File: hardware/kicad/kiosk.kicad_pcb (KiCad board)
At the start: 2 copper layers, 158 x 116 mm, 19 parts, among them J10 TerminalBlock_MaiXu_MX126-5.0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, J11 TerminalBlock_MaiXu_MX126-5.0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, J13 PinHeader_1x09_P2.54mm_Vertic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, J3 PinSocket_1x14_P2.54mm_Vertic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, J4 PinSocket_1x06_P2.54mm_Vertic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, J5 PinSocket_1x04_P2.54mm_Vertic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, J6 PinSocket_1x06_P2.54mm_Vertic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, J7 PinSocket_1x07_P2.54mm_Vertic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, J9 PinHeader_1x03_P2.54mm_Vertic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, U1 ESP32-S3-CAM

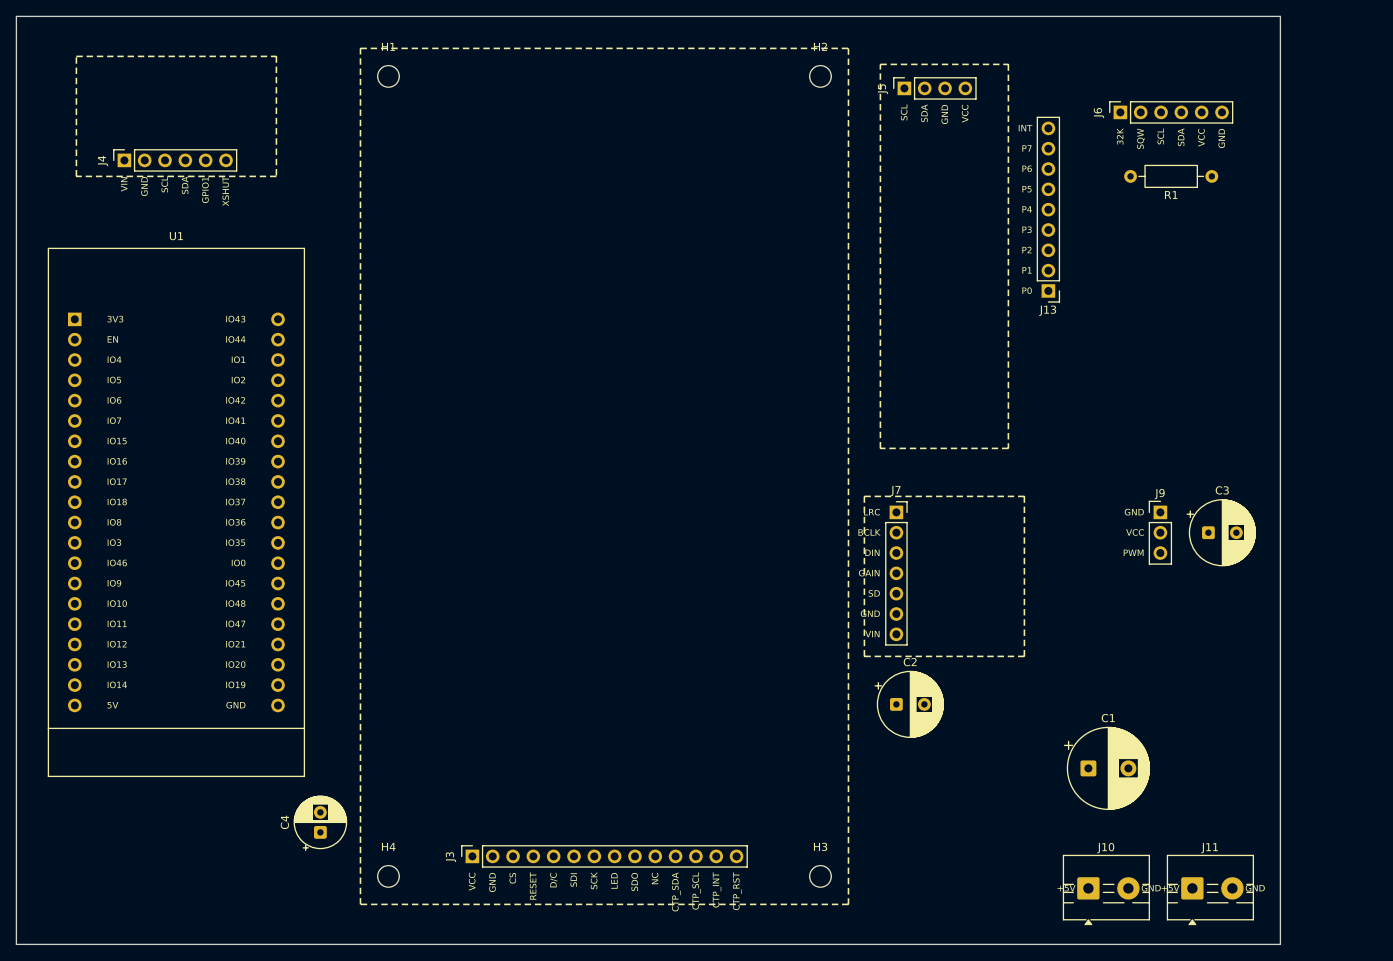
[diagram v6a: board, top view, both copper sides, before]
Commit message: fix(hardware): put the panel's header on the line its mounting holes sit on
Read off the module, the fourteen-pin row lands level with the two holes
at that end, about a millimetre nearer the edge. The board had it 2.5 mm
the other way. The two insets are therefore not independent: the header
one is now derived from the hole one, so the single measurement that is
still outstanding settles both at once, and there is no second number to
get wrong.

J3 drops to y 107.5 so the panel's far edge still clears the top of the
board. Its pin names now fall just below the panel's edge instead of
under it, which is where you want them: readable with the panel fitted.

Moving J11 inward last commit left the two supply terminals 1.5 mm apart,
and a label set beside a pad then reaches the neighbour: J10's GND landed
on J11's body, the same failure the outboard rule was written to fix. On
a two-pad row the label goes above its own pad now, nudged off the
reference text that sits centred between them.

Task: E14-T8
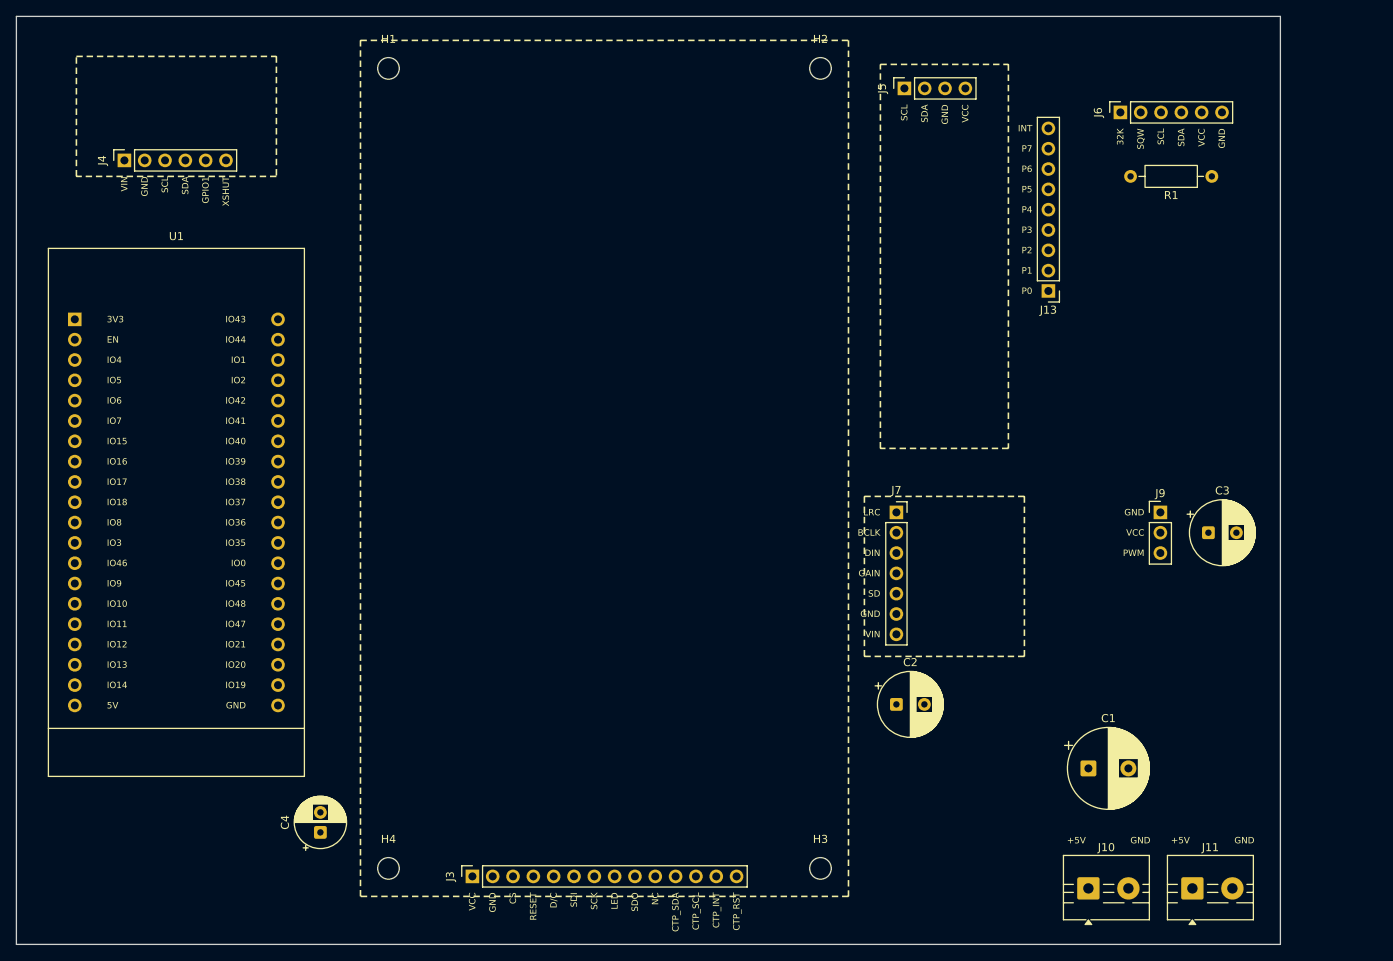
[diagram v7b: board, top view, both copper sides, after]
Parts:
- moved J3 2.50 mm to (57.0, 107.5)
- moved H1 1.00 mm to (46.5, 6.50)
- moved H2 1.00 mm to (100.5, 6.50)
- moved H3 1.00 mm to (100.5, 106.5)
- moved H4 1.00 mm to (46.5, 106.5)
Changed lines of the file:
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@@
 	(footprint "Connector_PinSocket_2.54mm:PinSocket_1x14_P2.54mm_Vertical"
 		(layer "F.Cu")
-		(at 57 105 90)
+		(at 57 107.5 90)
 		(descr "Through hole straight socket strip, 1x14, 2.54mm pitch, single row (from Kicad 4.0.7), script generated")
 		(tags "Through hole socket strip THT 1x14 2.54mm single row")
@@
 	(footprint "MountingHole:MountingHole_2.7mm"
 		(layer "F.Cu")
-		(at 100.51 7.5)
+		(at 100.51 6.5)
 		(descr "Mounting Hole 2.7mm, no annular, generated by kicad-footprint-generator mountinghole.py")
 		(tags "mountinghole")
@@
 	(footprint "MountingHole:MountingHole_2.7mm"
 		(layer "F.Cu")
-		(at 46.51 107.5)
+		(at 46.51 106.5)
 		(descr "Mounting Hole 2.7mm, no annular, generated by kicad-footprint-generator mountinghole.py")
 		(tags "mountinghole")
@@
 	(footprint "MountingHole:MountingHole_2.7mm"
 		(layer "F.Cu")
-		(at 100.51 107.5)
+		(at 100.51 106.5)
 		(descr "Mounting Hole 2.7mm, no annular, generated by kicad-footprint-generator mountinghole.py")
 		(tags "mountinghole")
@@
 	(footprint "MountingHole:MountingHole_2.7mm"
 		(layer "F.Cu")
-		(at 46.51 7.5)
+		(at 46.51 6.5)
 		(descr "Mounting Hole 2.7mm, no annular, generated by kicad-footprint-generator mountinghole.py")
 		(tags "mountinghole")
@@
 	)
 	(gr_line
-		(start 43.01 4)
-		(end 104.01 4)
+		(start 43.01 3)
+		(end 104.01 3)
 		(stroke
 			(width 0.2)
@@
 	)
 	(gr_line
-		(start 43.01 111)
-		(end 43.01 4)
+		(start 43.01 110)
+		(end 43.01 3)
 		(stroke
 			(width 0.2)
@@
 	)
 	(gr_line
-		(start 104.01 4)
-		(end 104.01 111)
+		(start 104.01 3)
+		(end 104.01 110)
 		(stroke
 			(width 0.2)
@@
 	)
 	(gr_line
-		(start 104.01 111)
-		(end 43.01 111)
+		(start 104.01 110)
+		(end 43.01 110)
 		(stroke
 			(width 0.2)
@@
 		)
 	)
+	(gr_text "+5V"
+		(at 132.5 103 0)
+		(layer "F.SilkS")
+		(effects
+			(font
+				(size 0.8 0.8)
+				(thickness 0.12)
+			)
+		)
+	)
 	(gr_text "GND"
-		(at 140.6 109 0)
+		(at 140.5 103 0)
+		(layer "F.SilkS")
+		(effects
+			(font
+				(size 0.8 0.8)
+				(thickness 0.12)
+			)
+		)
+	)
+	(gr_text "+5V"
+		(at 145.5 103 0)
 		(layer "F.SilkS")
 		(effects
@@
 				(thickness 0.12)
 			)
-			(justify left)
 		)
 	)
 	(gr_text "GND"
-		(at 153.6 109 0)
+		(at 153.5 103 0)
 		(layer "F.SilkS")
 		(effects
@@
 				(thickness 0.12)
 			)
-			(justify left)
 		)
 	)
@@
 		)
 	)
-	(gr_text "+5V"
-		(at 132.4 109 0)
-		(layer "F.SilkS")
-		(effects
-			(font
-				(size 0.8 0.8)
-				(thickness 0.12)
-			)
-			(justify right)
-		)
-	)
 	(gr_text "GND"
 		(at 141 62 0)
@@
 		)
 	)
-	(gr_text "+5V"
-		(at 145.4 109 0)
-		(layer "F.SilkS")
-		(effects
-			(font
-				(size 0.8 0.8)
-				(thickness 0.12)
-			)
-			(justify right)
-		)
-	)
 	(gr_text "VIN"
 		(at 13.5 20 90)
@@
 	)
 	(gr_text "VCC"
-		(at 57 107 90)
+		(at 57 109.5 90)
 		(layer "F.SilkS")
 		(effects
@@
 	)
 	(gr_text "GND"
-		(at 59.54 107 90)
+		(at 59.54 109.5 90)
 		(layer "F.SilkS")
 		(effects
@@
 	)
 	(gr_text "CS"
-		(at 62.08 107 90)
+		(at 62.08 109.5 90)
 		(layer "F.SilkS")
 		(effects
@@
 	)
 	(gr_text "RESET"
-		(at 64.62 107 90)
+		(at 64.62 109.5 90)
 		(layer "F.SilkS")
 		(effects
@@
 	)
 	(gr_text "D/C"
-		(at 67.16 107 90)
+		(at 67.16 109.5 90)
 		(layer "F.SilkS")
 		(effects
@@
 	)
 	(gr_text "SDI"
-		(at 69.7 107 90)
+		(at 69.7 109.5 90)
 		(layer "F.SilkS")
 		(effects
@@
 	)
 	(gr_text "SCK"
-		(at 72.24 107 90)
+		(at 72.24 109.5 90)
 		(layer "F.SilkS")
 		(effects
@@
 	)
 	(gr_text "LED"
-		(at 74.78 107 90)
+		(at 74.78 109.5 90)
 		(layer "F.SilkS")
 		(effects
@@
 	)
 	(gr_text "SDO"
-		(at 77.32 107 90)
+		(at 77.32 109.5 90)
 		(layer "F.SilkS")
 		(effects
@@
 	)
 	(gr_text "NC"
-		(at 79.86 107 90)
+		(at 79.86 109.5 90)
 		(layer "F.SilkS")
 		(effects
@@
 	)
 	(gr_text "CTP_SDA"
-		(at 82.4 107 90)
+		(at 82.4 109.5 90)
 		(layer "F.SilkS")
 		(effects
@@
 	)
 	(gr_text "CTP_SCL"
-		(at 84.94 107 90)
+		(at 84.94 109.5 90)
 		(layer "F.SilkS")
 		(effects
@@
 	)
 	(gr_text "CTP_INT"
-		(at 87.48 107 90)
+		(at 87.48 109.5 90)
 		(layer "F.SilkS")
 		(effects
@@
 	)
 	(gr_text "CTP_RST"
-		(at 90.02 107 90)
+		(at 90.02 109.5 90)
 		(layer "F.SilkS")
 		(effects

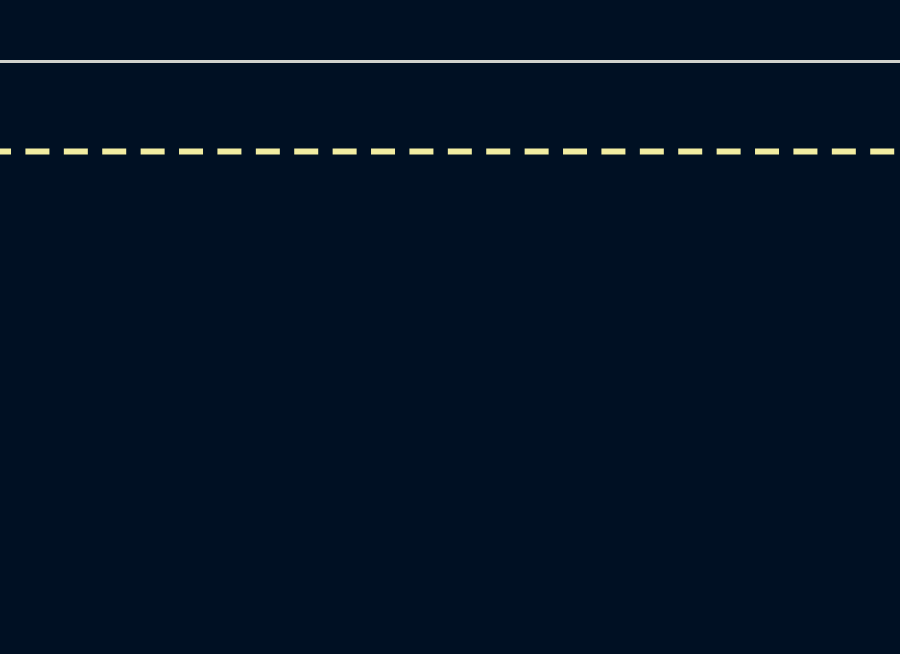
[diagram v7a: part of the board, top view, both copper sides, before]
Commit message: feat(hardware): land the panel's microSD row as four bare holes
J14 drills the four pins the panel carries on its far edge and connects
none of them. Drilling without connecting is nearly free; not drilling is
final, because the board is printed before anyone finds out whether that
row came populated, and a pin soldered there holds the panel off its
8.5 mm standoffs and leaves the four screws bending it instead of
holding it. The holes also take a soldered wire later, which is the same
job J13 already does for the expander's port row.

They stay unconnected because SD_CS has no pin to reach: the other three
would share SPI2 with the panel itself, but section 2.4 is out of ordinary
GPIO and the only candidate is GPIO48, which costs the status LED and is
therefore a section 1.2 decision, not a routing one.

Position is assumed centred on the far edge, mirroring the header on the
near one, and clears both top mounting holes by 20 mm. A few millimetres
of error costs nothing while the holes are only a place to solder a wire.

Task: E14-T8
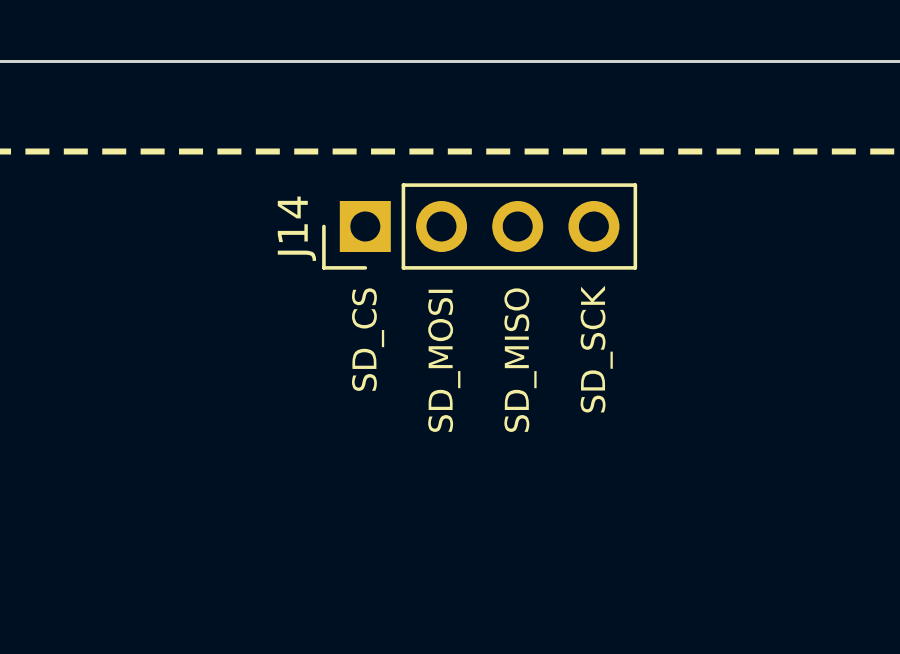
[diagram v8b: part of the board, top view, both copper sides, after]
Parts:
- added J14: PinHeader_1x04_P2.54mm_Vertical, Connector_PinHeader_2.54mm:PinHeader_1x04_P2.54mm_Vertical, F.Cu at (69.7, 5.50)
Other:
- board text added: "SD_CS"
- board text added: "SD_MISO"
- board text added: "SD_MOSI"
- board text added: "SD_SCK"
